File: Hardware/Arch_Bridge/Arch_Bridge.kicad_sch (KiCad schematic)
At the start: 87 parts, among them J1 Conn_01x02, J3 Conn_01x04, J4 Conn_01x04, Q1 2N3904, Q2 MJE2955, Q3 MJE2955, U1 AP63205WU, U11 ESP32-S3-WROOM-1, U12 TXS0102DCT, U13 DRV8231ADDAR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

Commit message: Completed BOM, PCB layout cleanup, starting software.
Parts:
- removed U?: 74AHC1G04, Package_TO_SOT_SMD:SOT-23-5_HandSoldering, symbol Loconet DCC Interface-rescue:74AHC1G04-74xGxx
- added U?: 74LVC1G04, Package_TO_SOT_SMD:SOT-23-5_HandSoldering, symbol Loconet DCC Interface-rescue:74AHC1G04-74xGxx
- CB1: MFG (none) -> Wuerth Electronik; PN (none) -> 865080545012
- D1, D2, D4: MFG (none) -> Wurth Elektronik
- DCC_IN? (x2), J3, J4: MFG (none) -> 3M; PN (none) -> 929850-01-04-RA
- F4: footprint Fuse:Fuse_1812_4532Metric_Pad1.30x3.40mm_HandSolder -> Fuse:Fuse_Bourns_MF-RHT200; MFG (none) -> Bourns; PN (none) -> MF-RHT200/32-2
- I2C_1, TTY_1: MFG (none) -> 3M; PN (none) -> 929850-01-03-RA
- J1: MFG (none) -> Wuerth Electronik; PN (none) -> 691322310002
- JP1: MFG (none) -> TE Connectivity; PN (none) -> 87224-2
- JP2, JP3: MFG (none) -> TE Connectivity; PN (none) -> 87224-3
- LOCONET_B1, LOCONET_B2, LOCONET_T1: MFG (none) -> Amphenol; PN (none) -> 54601-906WPLF
- Q1: MFG (none) -> Diotec Semiconductor; PN (none) -> 2N3904
- Q2, Q3: MFG (none) -> Onsemi; PN (none) -> MJE2955TG
- R1, R8: PN RT1206FRE071KL -> RC1206FR-071KL
- R11: PN RT1206FRE0733KL -> RC1206FR-0733KL
- R12, R15: PN RT1206FRE073KL -> RC1206FR-073KL
- R16, R17, R19, R20, R21, R22, R23, R6: PN RT1206FRD0710KL -> RC1206FR-1310KL
- R2: PN RT1206FRE074K7L -> RC1206FR-0747KL
- R3: PN RT1206FRE0747KL -> RC1206FR-0747KL
- R4: PN RT1206FRE07150KL -> RC1206FR-07150KL
- R5: PN RT1206FRE0722KL -> RC1206FR-0722KL
- R7: PN RT1206FRE07220KL -> RC1206FR-07220KL
- U11: MFG (none) -> Expressif; PN (none) -> ESP32-S3-WROOM-1U-N16
- U13, U7: MFG (none) -> Texas Insturments; PN (none) -> DRV8231ADDAR
- U19, U20: MFG (none) -> Texas Insturments; PN (none) -> TXS0108EPWR
- U3: value LM393 -> LM393B; MFG (none) -> Texas Insturments; PN (none) -> LM393BIDR
- U4, U?: value 74AHC1G04 -> 74LVC1G04; MFG (none) -> Texas Insturments; PN (none) -> SN74LVC1G04DBVR
- U5: value 74AHCT1G02 -> 74LVC1G02; MFG (none) -> Texas Insturments; PN (none) -> SN74LVC1G02DBVR
- U6: MFG (none) -> Toshiba; PN (none) -> TLP2770(TP,E
- U? (x4): MFG (none) -> Texas Insturments; PN (none) -> SN74LVC1G3208DBVR
- USB1: MFG (none) -> Molex; PN (none) -> 105017-0001
- V12: MFG (none) -> Eaton; PN (none) -> A202202
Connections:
- net +5V: now also U?.5 (VCC)
- net DCC_2: now also U?.2
- net GND: now also U?.3 (GND)
- net at U?.1: now also U?.4

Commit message: Revised L1 for possible 2A output, cleaner fill zones, fabrication outputs
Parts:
- L1: footprint Inductor_SMD:L_1008_2520Metric_Pad1.43x2.20mm_HandSolder -> Inductor_SMD_Wurth:L_Wurth_WE-LQSH-4020; MFG Murata Electronics -> Wuerth Electronik; PN LQM2HPN4R7MGCL -> 74405042047
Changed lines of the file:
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@@
       (effects (font (size 1.27 1.27)))
     )
-    (property "Footprint" "Inductor_SMD:L_1008_2520Metric_Pad1.43x2.20mm_HandSolder" (at 227.33 25.4 0)
+    (property "Footprint" "Inductor_SMD_Wurth:L_Wurth_WE-LQSH-4020" (at 227.33 25.4 0)
       (effects (font (size 1.27 1.27)) hide)
     )
-    (property "Datasheet" "https://www.mouser.com/datasheet/2/281/1/JELF243B_0025-1634213.pdf" (at 227.33 25.4 0)
+    (property "Datasheet" "" (at 227.33 25.4 0)
       (effects (font (size 1.27 1.27)) hide)
     )
-    (property "MFG" "Murata Electronics" (at 227.33 25.4 0)
+    (property "MFG" "Wuerth Electronik" (at 227.33 25.4 0)
       (effects (font (size 1.27 1.27)) hide)
     )
-    (property "PN" "LQM2HPN4R7MGCL " (at 227.33 25.4 0)
+    (property "PN" "74405042047" (at 227.33 25.4 0)
       (effects (font (size 1.27 1.27)) hide)
     )

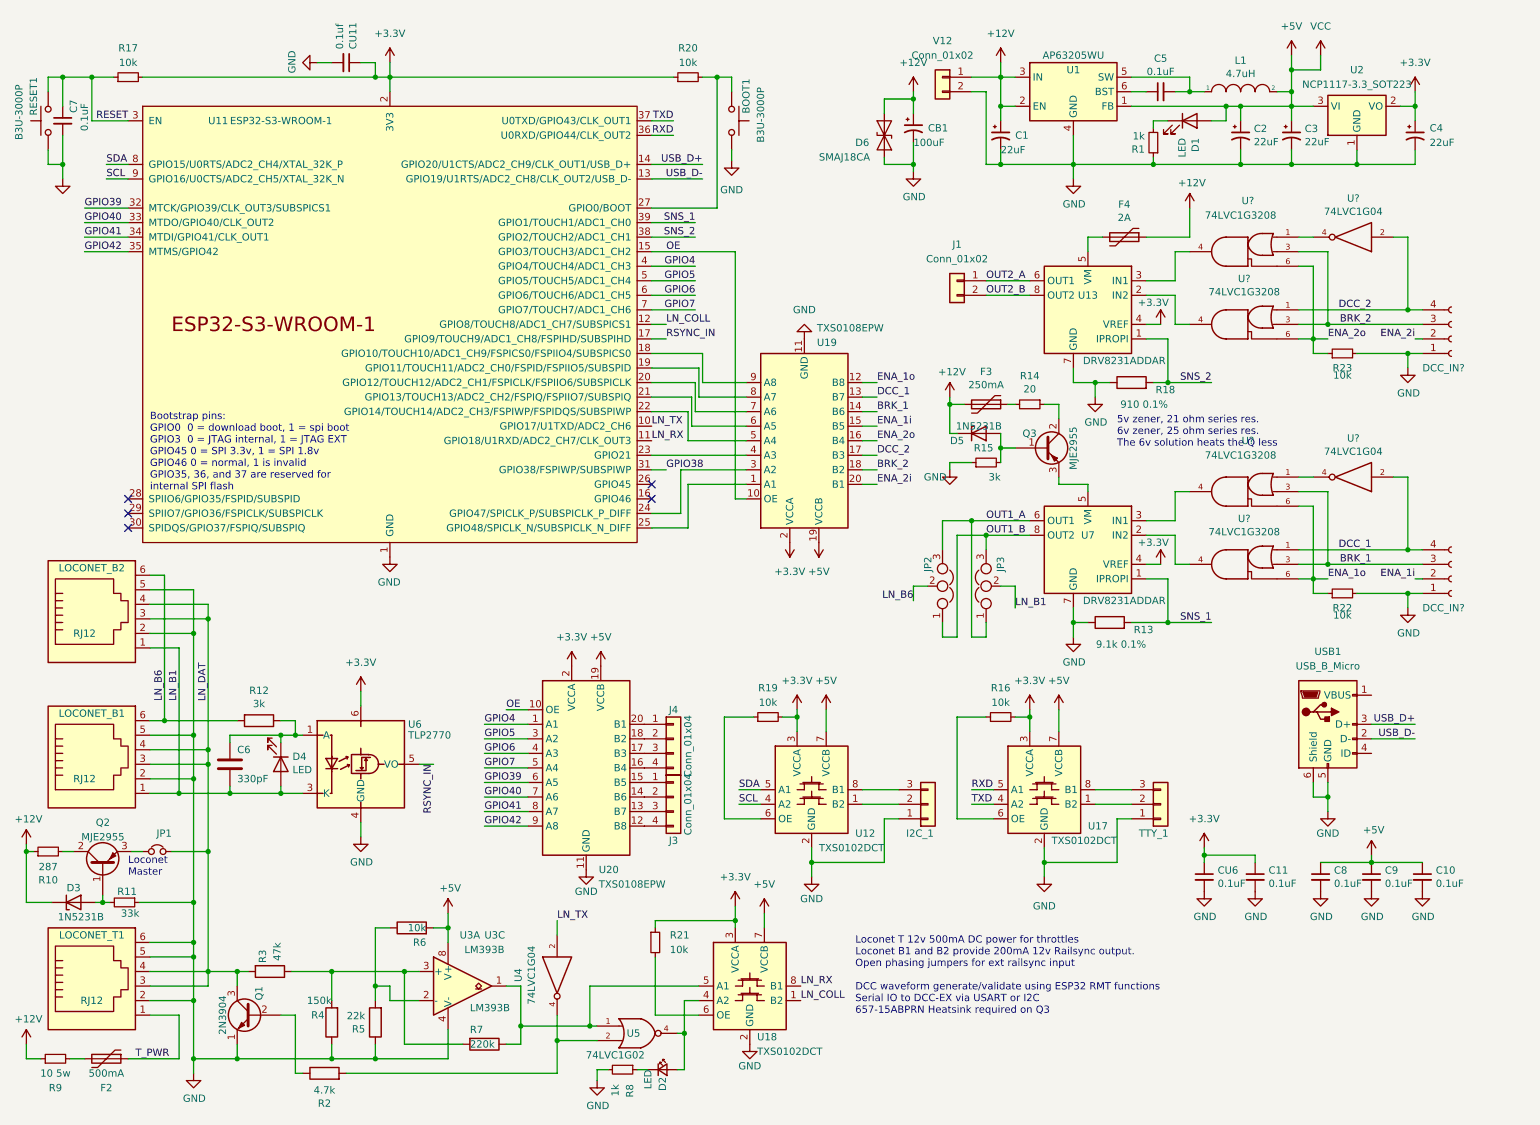
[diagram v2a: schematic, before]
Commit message: BOM Cleanup, substitute 3.3v LDO for easier to get part.
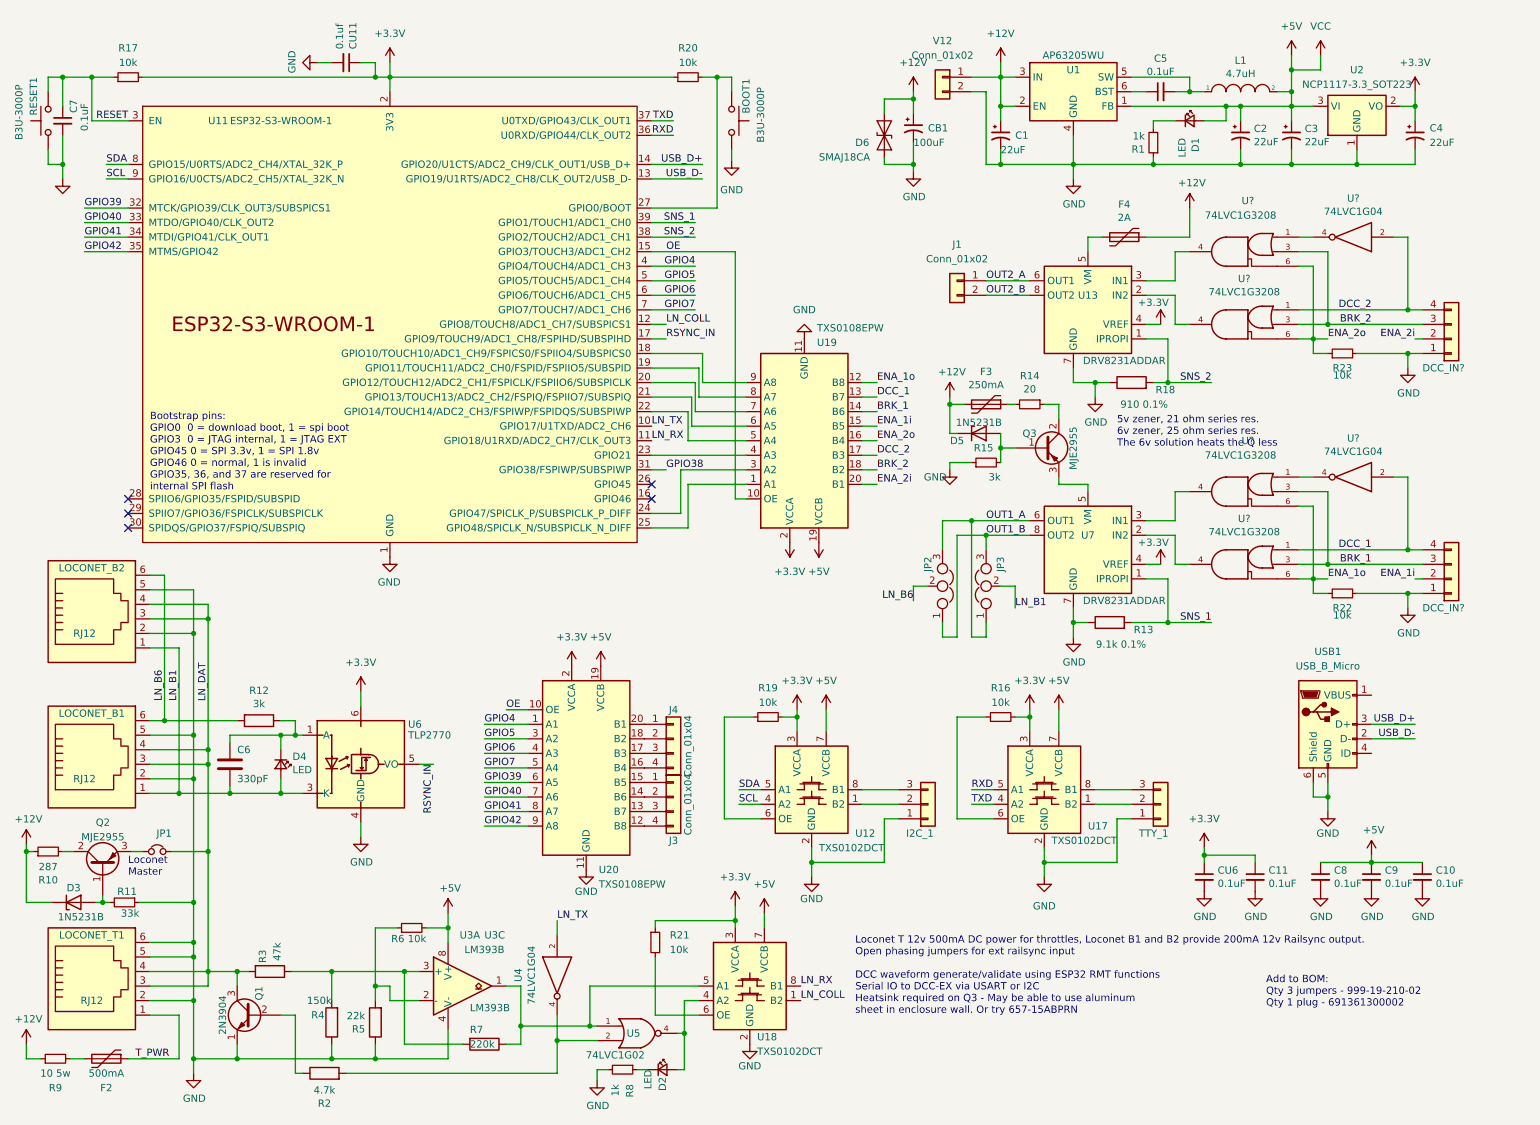
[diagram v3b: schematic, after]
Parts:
- C1, C2, C3: symbol Motor Shield Adapter-rescue:CP1_Small-Device -> Device:C_Polarized_Small_US
- D1, D4: symbol Device:LED -> Device:LED_Small
- DCC_IN? (x2): symbol Loconet DCC Interface-rescue:Conn_01x04_Female-Connector -> Connector_Generic:Conn_01x04
- R10: PN SQM500JB-10R -> RC1206FR-07287RL
- R6: symbol Device:R -> Device:R_Small
- U2: MFG ONSemi -> Texas Insturments; PN NCP1117ST33T3G -> TLV1117-33CDCYR
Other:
- note added: "Add to BOM: Qty 3 jumpers - 999-19-210-02 Qty 1 plug - 691361300002"
- note added: "Loconet T 12v 500mA DC power for throttles, Loconet B1 and B2 provide 200mA 12v Railsync output. Open phasing jumpers for ext railsync input DCC waveform generate/validate using ESP32 RMT functions Serial IO to DCC-EX via USART or I2C Heatsink required on Q3 - May be able to use aluminum sheet in enclosure wall. Or try 657-15ABPRN"
- note removed: "Loconet T 12v 500mA DC power for throttles Loconet B1 and B2 provide 200mA 12v Railsync output. Open phasing jumpers for ext railsync input DCC waveform generate/validate using ESP32 RMT functions Serial IO to DCC-EX via USART or I2C 657-15ABPRN Heatsink required on Q3"
- moved on the sheet: D1, D4
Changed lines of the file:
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@@
     (stroke (width 0) (type default))
   )
+  (wire (pts (xy 59.69 145.415) (xy 59.69 147.955))
+    (stroke (width 0) (type default))
+  )
   (wire (pts (xy 242.57 113.03) (xy 240.03 113.03))
     (stroke (width 0) (type default))
@@
     (stroke (width 0) (type default))
   )
+  (wire (pts (xy 220.98 30.48) (xy 224.79 30.48))
+    (stroke (width 0) (type default))
+  )
   (wire (pts (xy 44.45 120.015) (xy 44.45 137.795))
     (stroke (width 0) (type default))
@@
     (stroke (width 0) (type default))
   )
-  (wire (pts (xy 86.36 171.45) (xy 88.9 171.45))
+  (wire (pts (xy 85.09 171.45) (xy 88.9 171.45))
     (stroke (width 0) (type default))
   )
@@
     (stroke (width 0) (type default))
   )
-  (wire (pts (xy 59.69 147.955) (xy 59.69 146.685))
-    (stroke (width 0) (type default))
-  )
   (wire (pts (xy 177.8 102.87) (xy 177.8 120.65))
     (stroke (width 0) (type default))
@@
     (stroke (width 0) (type default))
   )
-  (wire (pts (xy 59.69 137.795) (xy 59.69 139.065))
+  (wire (pts (xy 59.69 137.795) (xy 59.69 140.335))
     (stroke (width 0) (type default))
   )
@@
     (stroke (width 0) (type default))
   )
-  (wire (pts (xy 214.63 30.48) (xy 212.09 30.48))
+  (wire (pts (xy 212.09 30.48) (xy 215.9 30.48))
     (stroke (width 0) (type default))
   )
@@
     (stroke (width 0) (type default))
   )
-  (wire (pts (xy 78.74 171.45) (xy 76.2 171.45))
+  (wire (pts (xy 76.2 171.45) (xy 80.01 171.45))
     (stroke (width 0) (type default))
   )
@@
     (stroke (width 0) (type default))
   )
-  (wire (pts (xy 222.25 30.48) (xy 224.79 30.48))
-    (stroke (width 0) (type default))
-  )
   (wire (pts (xy 152.4 160.02) (xy 152.4 162.56))
     (stroke (width 0) (type default))
@@
     (stroke (width 0) (type default))
   )
-  (text "Loconet T 12v 500mA DC power for throttles\nLoconet B1 and B2 provide 200mA 12v Railsync output.\nOpen phasing jumpers for ext railsync input\n\nDCC waveform generate/validate using ESP32 RMT functions\nSerial IO to DCC-EX via USART or I2C\n657-15ABPRN Heatsink required on Q3\n"
+  (text "Loconet T 12v 500mA DC power for throttles, Loconet B1 and B2 provide 200mA 12v Railsync output.\nOpen phasing jumpers for ext railsync input\n\nDCC waveform generate/validate using ESP32 RMT functions\nSerial IO to DCC-EX via USART or I2C\nHeatsink required on Q3 - May be able to use aluminum\nsheet in enclosure wall. Or try 657-15ABPRN \n"
     (at 160.02 186.69 0)
     (effects (font (size 1.27 1.27)) (justify left bottom))
@@
     (effects (font (size 1.27 1.27)) (justify left bottom))
   )
+  (text "Add to BOM: \nQty 3 jumpers - 999-19-210-02\nQty 1 plug - 691361300002"
+    (at 231.775 185.42 0)
+    (effects (font (size 1.27 1.27)) (justify left bottom))
+  )
   (text "5v zener, 21 ohm series res.\n6v zener, 25 ohm series res.\nThe 6v solution heats the Q less"
     (at 205.74 87.63 0)
@@
     )
   )
-  (symbol (lib_id "Device:LED") (at 59.69 142.875 270) (unit 1)
+  (symbol (lib_id "Device:LED_Small") (at 59.69 142.875 270) (unit 1)
     (in_bom yes) (on_board yes) (dnp no)
     (property "Reference" "D4" (at 61.722 141.5288 90)
@@
       (effects (font (size 1.27 1.27)) (justify left))
     )
-    (property "Footprint" "LED_SMD:LED_1206_3216Metric" (at 59.69 142.875 0)
+    (property "Footprint" "LED_SMD:LED_1206_3216Metric" (at 59.69 142.875 90)
       (effects (font (size 1.27 1.27)) hide)
     )
-    (property "Datasheet" "https://www.mouser.com/datasheet/2/445/156120RS75300-1715573.pdf" (at 59.69 142.875 0)
+    (property "Datasheet" "" (at 59.69 142.875 90)
       (effects (font (size 1.27 1.27)) hide)
     )
@@
     )
   )
-  (symbol (lib_id "Device:R") (at 82.55 171.45 90) (unit 1)
+  (symbol (lib_id "Device:R_Small") (at 82.55 171.45 90) (unit 1)
     (in_bom yes) (on_board yes) (dnp no)
-    (property "Reference" "R6" (at 85.09 173.99 90)
+    (property "Reference" "R6" (at 81.28 173.355 90)
       (effects (font (size 1.27 1.27)) (justify left))
     )
-    (property "Value" "10k" (at 85.09 171.45 90)
+    (property "Value" "10k" (at 85.09 173.355 90)
       (effects (font (size 1.27 1.27)) (justify left))
     )
-    (property "Footprint" "Resistor_SMD:R_1206_3216Metric" (at 82.55 173.228 90)
+    (property "Footprint" "Resistor_SMD:R_1206_3216Metric" (at 82.55 171.45 0)
       (effects (font (size 1.27 1.27)) hide)
     )
-    (property "Datasheet" "https://www.mouser.com/datasheet/2/54/cr-1858361.pdf" (at 82.55 171.45 0)
+    (property "Datasheet" "~" (at 82.55 171.45 0)
       (effects (font (size 1.27 1.27)) hide)
     )
@@
       (effects (font (size 1.27 1.27)))
     )
-    (property "Value" "1N5231B" (at 181.61 83.82 0)
+    (property "Value" "1N5231B" (at 181.61 83.185 0)
       (effects (font (size 1.27 1.27)))
     )
@@
       (effects (font (size 1.27 1.27)) hide)
     )
-    (property "PN" "SQM500JB-10R " (at 19.05 158.115 0)
+    (property "PN" "RC1206FR-07287RL" (at 19.05 158.115 0)
       (effects (font (size 1.27 1.27)) hide)
     )
@@
       (effects (font (size 1.27 1.27)) hide)
     )
-    (property "MFG" "ONSemi" (at 247.65 27.94 0)
+    (property "MFG" "Texas Insturments" (at 247.65 27.94 0)
       (effects (font (size 1.27 1.27)) hide)
     )
-    (property "PN" "NCP1117ST33T3G" (at 247.65 27.94 0)
+    (property "PN" "TLV1117-33CDCYR" (at 247.65 27.94 0)
       (effects (font (size 1.27 1.27)) hide)
     )
@@
     )
   )
-  (symbol (lib_id "Motor Shield Adapter-rescue:CP1_Small-Device") (at 185.42 33.02 0) (unit 1)
+  (symbol (lib_id "Device:C_Polarized_Small_US") (at 185.42 33.02 0) (unit 1)
     (in_bom yes) (on_board yes) (dnp no)
     (property "Reference" "C1" (at 187.96 33.02 0)
@@
     )
   )
-  (symbol (lib_id "Device:LED") (at 218.44 30.48 0) (unit 1)
+  (symbol (lib_id "Device:LED_Small") (at 218.44 30.48 0) (unit 1)
     (in_bom yes) (on_board yes) (dnp no)
     (property "Reference" "D1" (at 219.4306 33.4772 90)
@@
       (effects (font (size 1.27 1.27)) (justify right))
     )
-    (property "Footprint" "LED_SMD:LED_1206_3216Metric" (at 218.44 30.48 0)
+    (property "Footprint" "LED_SMD:LED_1206_3216Metric" (at 218.44 30.48 90)
       (effects (font (size 1.27 1.27)) hide)
     )
-    (property "Datasheet" "https://www.mouser.com/datasheet/2/445/156120RS75300-1715573.pdf" (at 218.44 30.48 0)
+    (property "Datasheet" "" (at 218.44 30.48 90)
       (effects (font (size 1.27 1.27)) hide)
     )
@@
     )
   )
-  (symbol (lib_id "Loconet DCC Interface-rescue:Conn_01x04_Female-Connector") (at 264.16 68.58 0) (mirror x) (unit 1)
+  (symbol (lib_id "Connector_Generic:Conn_01x04") (at 264.16 68.58 0) (mirror x) (unit 1)
     (in_bom yes) (on_board yes) (dnp no)
     (property "Reference" "DCC_IN?" (at 259.08 73.66 0)
@@
     )
   )
-  (symbol (lib_id "Motor Shield Adapter-rescue:CP1_Small-Device") (at 227.33 33.02 0) (unit 1)
+  (symbol (lib_id "Device:C_Polarized_Small_US") (at 227.33 33.02 0) (unit 1)
     (in_bom yes) (on_board yes) (dnp no)
     (property "Reference" "C2" (at 229.6414 31.8516 0)
@@
     )
   )
-  (symbol (lib_id "Loconet DCC Interface-rescue:Conn_01x04_Female-Connector") (at 264.16 110.49 0) (mirror x) (unit 1)
+  (symbol (lib_id "Connector_Generic:Conn_01x04") (at 264.16 110.49 0) (mirror x) (unit 1)
     (in_bom yes) (on_board yes) (dnp no)
     (property "Reference" "DCC_IN?" (at 259.08 115.57 0)
@@
     )
   )
-  (symbol (lib_id "Motor Shield Adapter-rescue:CP1_Small-Device") (at 236.22 33.02 0) (unit 1)
+  (symbol (lib_id "Device:C_Polarized_Small_US") (at 236.22 33.02 0) (unit 1)
     (in_bom yes) (on_board yes) (dnp no)
     (property "Reference" "C3" (at 238.5314 31.8516 0)
@@
       (effects (font (size 1.27 1.27)) hide)
     )
-    (property "Datasheet" "https://www.mouser.com/datasheet/2/445/156120RS75300-1715573.pdf" (at 126.365 196.215 90)
+    (property "Datasheet" "" (at 126.365 196.215 90)
       (effects (font (size 1.27 1.27)) hide)
     )
